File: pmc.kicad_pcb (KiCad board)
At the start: 6 copper layers, 52.1 x 93.3 mm, 164 parts, among them M1 LM46001, M2 TPS61040, M3 STM32F405RG, M4 REF3033, M5 TPS73633, M6 SN65HVD233, M7 UCC27211A, M8 UCC27211A, M9 UCC27211A, P1 BOOT, P10 CONN4, P11 FAN, P12 F1, P13 F2, P14 A1, P15 A2, P16 F1, P17 F2, P18 A1, P19 A2, P2 PPM, P20 ANALOG, P21 SWD, P22 USART, P23 HALL, P3 NTC, P4 SPI, P5 CAN, P6 CONN4, P7 CONN4, P8 CONN4, P9 CONN4, Q1 IRLML6401, Q2 IPT007N06N, Q3 IPT007N06N, Q4 IPT007N06N, Q5 IPT007N06N, Q6 IPT007N06N, Q7 IPT007N06N, U1 AD8539, U2 AD8539, U3 AD8417, U4 AD8417

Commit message: New annotation.
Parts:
- renumbered C62 to C1, C16 to C10, C3 to C11, C7 to C12, C39 to C13, C8 to C14, C9 to C15, C21 to C16, C22 to C17, C12 to C18, C24 to C19, C17 to C20, C40 to C21, C18 to C22, C27 to C23, C13 to C24, C14 to C25, C43 to C26, C19 to C27, C23 to C28, C20 to C29, C10 to C3, C25 to C30, C26 to C31, C28 to C32, C30 to C33, C31 to C34, C41 to C35, C42 to C36, C32 to C37, C33 to C38, C34 to C39, C11 to C4, C29 to C40, C35 to C41, C36 to C42, C37 to C43, C38 to C44, C44 to C45, C45 to C46, C46 to C47, C47 to C48, C48 to C49, C1 to C5, C49 to C50, C50 to C51, C51 to C52, C52 to C53, C53 to C54, C54 to C55, C55 to C56, C56 to C57, C57 to C58, C58 to C59, C4 to C6, C59 to C60, C64 to C61, C65 to C62, C66 to C63, C60 to C64, C61 to C65, C5 to C7, C6 to C8, C15 to C9, D2 to D1, D1 to D2, M2 to M1, M1 to M2, P11 to P1, P12 to P10, P13 to P11, P14 to P12, P15 to P13, P1 to P14, P16 to P15, P17 to P16, P18 to P17, P19 to P18, P6 to P19, P3 to P2, P7 to P20, P8 to P21, P9 to P22, P10 to P23, P23 to P3, P2 to P5, P20 to P6, P5 to P7, P21 to P8, P22 to P9, R34 to R1, R13 to R11, R14 to R12, R15 to R13, R40 to R14, R16 to R15, R17 to R16, R18 to R17, R42 to R18, R8 to R19, R19 to R2, R1 to R20, R3 to R21, R48 to R22, R20 to R23, R21 to R24, R22 to R25, R2 to R26, R4 to R27, R23 to R28, R24 to R29, R41 to R3, R25 to R30, R43 to R31, R44 to R32, R47 to R33, R49 to R34, R50 to R36, R26 to R37, R27 to R38, R28 to R39, R6 to R4, R29 to R40, R30 to R41, R31 to R42, R32 to R43, R33 to R44, R36 to R47, R37 to R48, R38 to R49, R39 to R50, R7 to R6, R11 to R7, R12 to R8
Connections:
- M2 pad 11: (no net) -> Net-(M2-Pad11)
- M2 pad 6: (no net) -> Net-(M2-Pad6)
- M2 pad 8: (no net) -> Net-(M2-Pad8)
- M3 pad 2: (no net) -> Net-(M3-Pad2)
- M3 pad 25: (no net) -> Net-(M3-Pad25)
- M3 pad 26: (no net) -> Net-(M3-Pad26)
- M3 pad 27: (no net) -> Net-(M3-Pad27)
- M3 pad 29: (no net) -> Net-(M3-Pad29)
- M3 pad 3: (no net) -> Net-(M3-Pad3)
- M3 pad 30: (no net) -> Net-(M3-Pad30)
- M3 pad 4: (no net) -> Net-(M3-Pad4)
- M3 pad 40: (no net) -> Net-(M3-Pad40)
- M3 pad 44: (no net) -> Net-(M3-Pad44)
- M3 pad 45: (no net) -> Net-(M3-Pad45)
- M3 pad 50: (no net) -> Net-(M3-Pad50)
- M3 pad 54: (no net) -> Net-(M3-Pad54)
- M3 pad 55: (no net) -> Net-(M3-Pad55)
- M3 pad 56: (no net) -> Net-(M3-Pad56)
- M3 pad 57: (no net) -> Net-(M3-Pad57)
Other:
- board text added: "(HALL/QEP)"
- board text added: "+50V"
- board text removed: "(HALL/ENCODER)"
- board text removed: "+40V"

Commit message: Updated to rev4c.
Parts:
- added R51: 820, foot:SM-1206, B.Cu at (66.7, 121.9)
- D1: moved to B.Cu
- D3: value NSR0320 -> 1N4448WS
- R33: value *NF -> 1
- R35: value 120 -> 820
- moved C58 18.1 mm to (70.5, 69.5), turned to 180 degrees
- moved C60 17.9 mm to (86.4, 69.5), turned to 0 degrees
- moved C65 17.8 mm to (102.2, 69.5), turned to 180 degrees
- moved C40 3.59 mm to (99.7, 123.8), turned to 270 degrees
- moved R36 2.54 mm to (103.5, 123.8)
- moved R2 2.01 mm to (76.8, 140.3), turned to 90 degrees
- moved D1 1.08 mm to (76.8, 140.3), turned to 90 degrees
- moved R34 0.64 mm to (101.6, 123.8), turned to 270 degrees
- moved C9 0.51 mm to (97.8, 139.6)
- moved R11 0.44 mm to (97.2, 143.5)
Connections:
- D1 pad 1: Net-(D1-Pad1) -> GND
- D1 pad 2: LED -> Net-(D1-Pad2)
- R2 pad 1: Net-(D1-Pad1) -> LED
- R2 pad 2: GND -> Net-(D1-Pad2)
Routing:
- net GND: track 402.6 -> 427.7 mm, vias 218 -> 219
- net +12V: track 71.7 -> 60.6 mm
- net +3.3V: track 42.9 -> 50.0 mm, vias 14 -> 13
- net Net-(M6-Pad7): track 7.82 -> 12.2 mm
- net Net-(M6-Pad6): track 7.82 -> 12.2 mm
- net Net-(P6-Pad2): track 2.73 -> 5.27 mm
- net (no net): track 0.00 -> 2.54 mm, vias 0 -> 5
- net Net-(D1-Pad1): track 2.24 -> 0.00 mm
- net Net-(D1-Pad2): track 0.00 -> 2.16 mm, vias 0 -> 1
- net ADC_IN14: track 30.2 -> 28.6 mm
- net NRST: track 41.5 -> 40.1 mm, vias 1 -> 0
- net LED: track 5.42 -> 6.24 mm
- net 12V_EN: track 16.5 -> 17.3 mm
- net FAN: track 10.8 -> 10.3 mm
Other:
- board text added: "(I2C/USART/PPM)"
- board text added: "L (CAN) H"
- board text added: "LED"
- board text removed: "10uH"
- board text removed: "22uH"

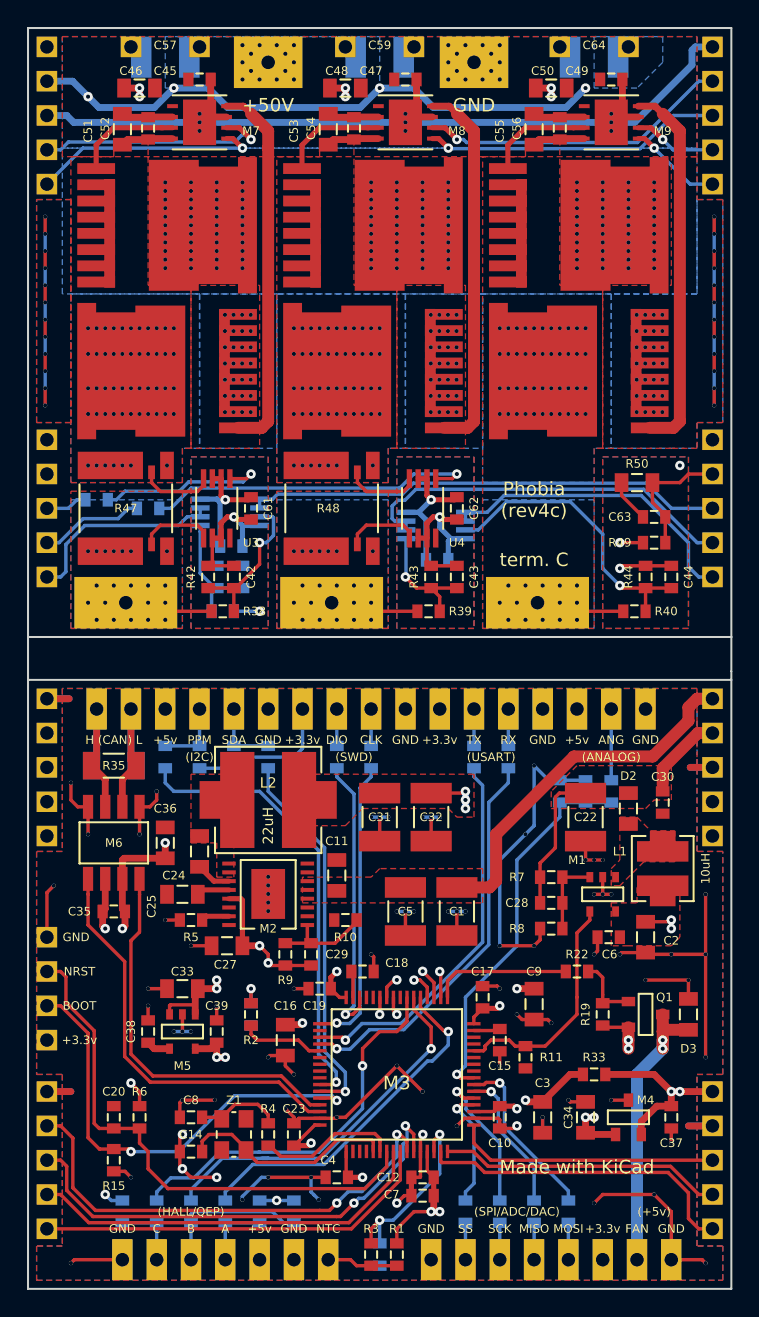
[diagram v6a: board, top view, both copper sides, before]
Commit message: Moved CAN to 5v, fixed filter capacitors, etc.
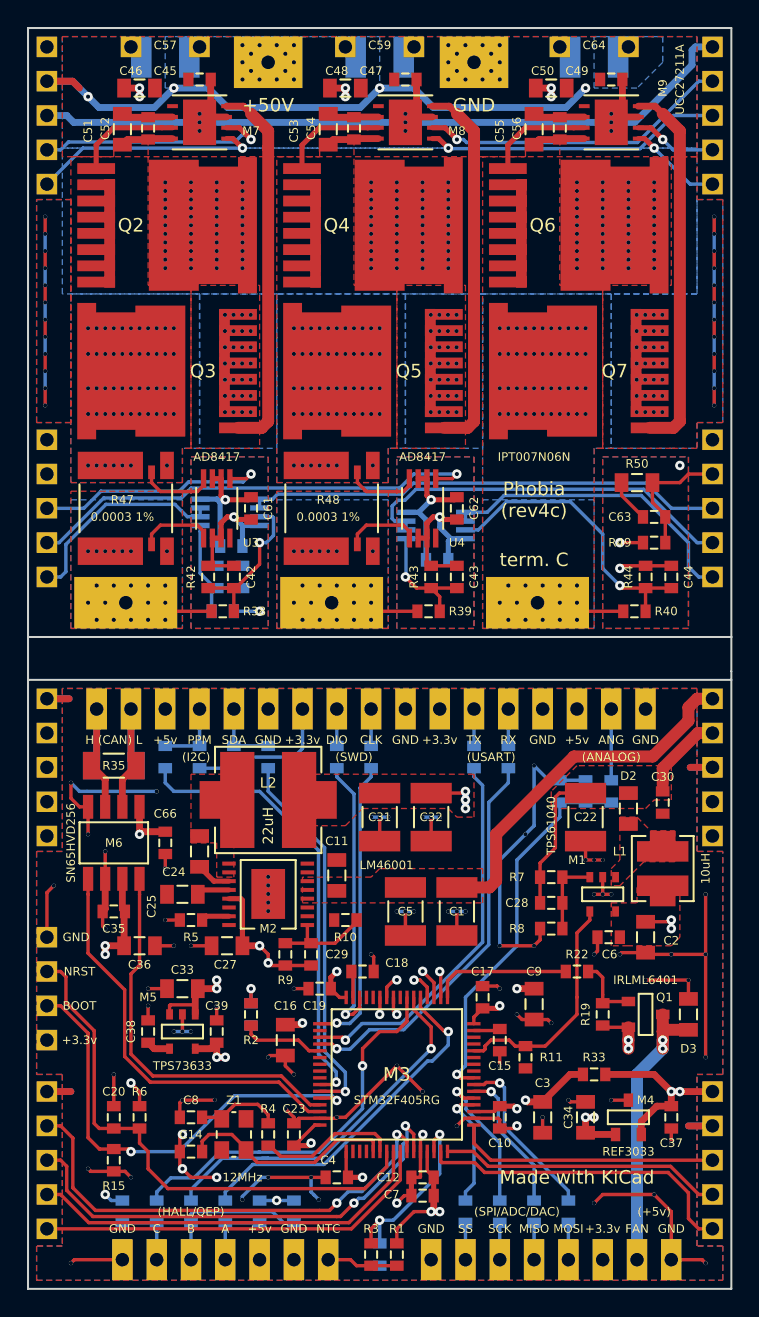
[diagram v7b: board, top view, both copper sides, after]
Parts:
- removed R45, R46: 1K 1%, foot:SM-0603
- added C66: 100nF 25v, foot:SM-0603, F.Cu at (70.5, 127.6)
- C41, C42, C43, C44: value 47pF C0G -> 1nF C0G
- M6: value SN65HVD233 -> SN65HVD256
- R8: value 11.3K 1% -> 13.7K 1%
- moved C36 7.85 mm to (68.6, 135.3), turned to 180 degrees
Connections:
- C35 pad 2: +3.3V -> +5V
- C36 pad 2: +3.3V -> +5V
- M6 pad 3: +3.3V -> +5V
- M6 pad 5: GND -> +3.3V
- P17 pad 3: Net-(P17-Pad3) -> CURRENT_A
- P17 pad 4: Net-(P17-Pad4) -> CURRENT_B
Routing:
- net GND: track 427.7 -> 441.5 mm, vias 219 -> 228
- net CURRENT_B: track 24.8 -> 34.9 mm
- net Net-(P17-Pad4): track 7.85 -> 0.00 mm
- net +5V: track 35.8 -> 42.9 mm, vias 15 -> 17
- net +3.3V: track 50.0 -> 44.4 mm, vias 13 -> 12
- net CURRENT_A: track 13.1 -> 17.9 mm
- net Net-(P17-Pad3): track 3.12 -> 0.00 mm
- net +12V: track 60.6 -> 63.2 mm
- net (no net): track 2.54 -> 0.00 mm, vias 5 -> 0
- net VOLTAGE_U: track 15.1 -> 15.9 mm

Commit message: Added voltage bias resistors.
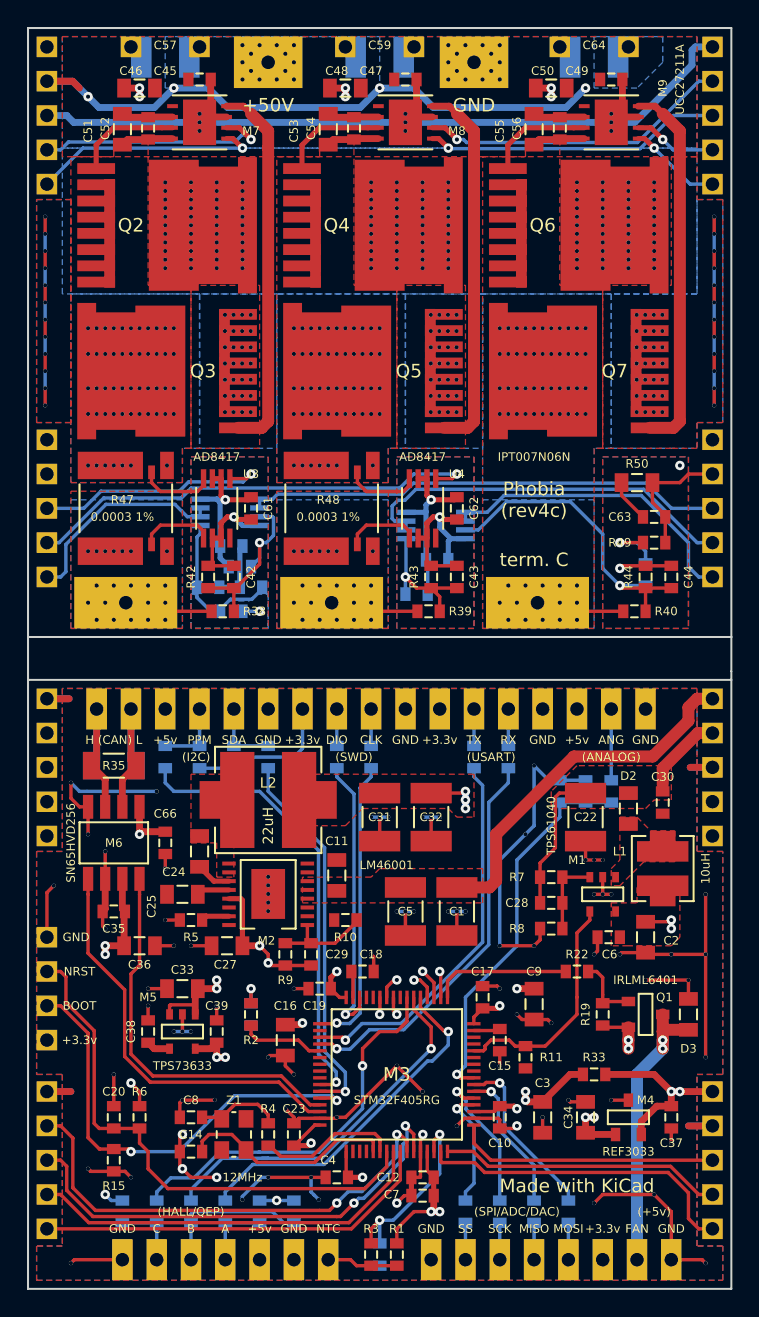
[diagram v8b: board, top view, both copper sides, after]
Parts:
- added R45: 470K 1%, foot:SM-0603, B.Cu at (76.0, 107.2)
- added R46: 470K 1%, foot:SM-0603, B.Cu at (89.1, 109.2)
- added R52: 470K 1%, foot:SM-0603, B.Cu at (106.0, 107.8)
- moved C41 0.99 mm to (73.7, 108.7), turned to 0 degrees
- moved R41 0.99 mm to (76.8, 108.7), turned to 0 degrees
- moved R37 0.63 mm to (75.4, 110.5)
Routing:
- net +3.3VREF: track 113.7 -> 121.4 mm
- net GND: track 441.5 -> 444.6 mm
- net Net-(C41-Pad1): track 8.99 -> 11.7 mm
- net Net-(C42-Pad1): track 11.5 -> 13.5 mm
- net Net-(C44-Pad1): track 22.0 -> 23.9 mm
- net Net-(C24-Pad1): track 0.00 -> 1.78 mm
- net +5V: track 42.9 -> 44.6 mm
- net Net-(C43-Pad1): track 8.98 -> 10.3 mm
- net +36V: track 189.5 -> 188.9 mm
- net +3.3V: track 44.4 -> 45.0 mm, vias 12 -> 13
